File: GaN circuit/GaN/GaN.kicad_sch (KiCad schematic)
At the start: 1 part, among them IC1 LTC7891RUFDM#PBF

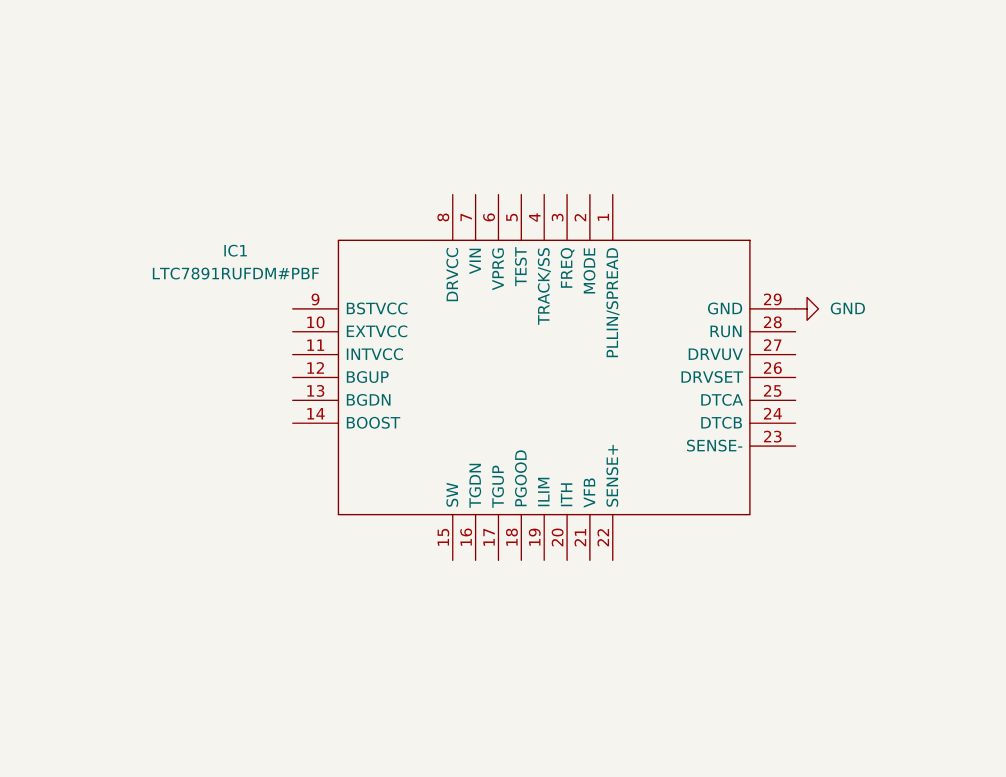
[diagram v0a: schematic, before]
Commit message: Began wiring the PCB for the GaN circuit
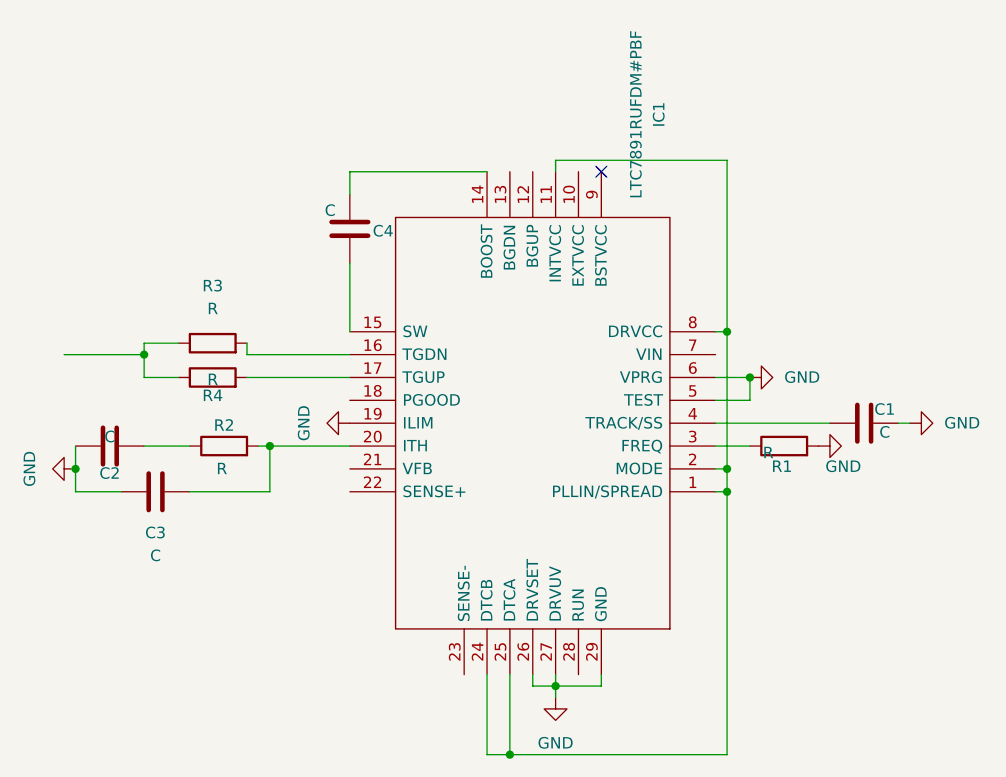
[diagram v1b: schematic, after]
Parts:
- added C1, C2, C3, C4: C, symbol Device:C
- added R1, R2, R3, R4: R, symbol Device:R
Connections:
- net GND: now also IC1.19 (ILIM), IC1.26 (DRVSET), IC1.27 (DRVUV), IC1.5 (TEST), IC1.6 (VPRG), C1.2, C2.1, C3.1, R1.2
- net at IC1.1 (PLLIN/SPREAD): now also IC1.11 (INTVCC), IC1.2 (MODE), IC1.24 (DTCB), IC1.25 (DTCA), IC1.8 (DRVCC)
- net at IC1.14 (BOOST): now also C4.1
- net at IC1.15 (SW): now also C4.2
- net at IC1.16 (TGDN): now also R3.2
- net at IC1.17 (TGUP): now also R4.2
- net at IC1.20 (ITH): now also C3.2, R2.2
- net at IC1.3 (FREQ): now also R1.1
- net at IC1.4 (TRACK/SS): now also C1.1
- new net: C2.2, R2.1
- new net: R3.1, R4.1
- no-connect marks 0 -> 1
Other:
- moved on the sheet: IC1

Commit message: Finished GaN schematic
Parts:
- removed R1: R, symbol Device:R
- added C10, C11, C14, C5, C6, C7, C8, C9: C, symbol Device:C
- added C12, C13, C15: C_US, symbol Device:C_US
- added L1: L, symbol Device:L
- added Q1, Q2: EPC2001C, EPC_FETs:D0188, symbol EPC_FETs:EPC2001C
- added R10, R11, R5, R6, R7, R8, R9: R, symbol Device:R
- added V2: 1, symbol Simulation_SPICE:VDC
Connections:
- net GND: now also IC1.1 (PLLIN/SPREAD), IC1.3 (FREQ), C10.2, C11.2, C12.2, C13.2, C14.2, C15.2, C5.1, C6.1, C8.2, C9.2, Q2.10 (S4), Q2.2 (Sub), Q2.4 (S1), Q2.6 (S2), Q2.8 (S3), R11.2, R9.2, V2.2; no longer IC1.19 (ILIM)
- net ITH: now reaches C3.2, IC1.20 (ITH), R2.2
- net at R3.1, R4.1: now also Q1.1 (G)
- net TGUP: now reaches IC1.17 (TGUP), R4.2
- net INTVCC: now reaches IC1.11 (INTVCC), IC1.2 (MODE), IC1.24 (DTCB), IC1.25 (DTCA), IC1.8 (DRVCC)
- net INTVCC: now also C6.2, R5.2; no longer IC1.1 (PLLIN/SPREAD)
- net OUT: now reaches IC1.10 (EXTVCC)
- net OUT: now also IC1.21 (VFB), IC1.23 (SENSE-), C10.1, C11.1, C12.1, C13.1, C7.2, C8.1, C9.1, R8.1, R9.1
- net BGUP: now reaches IC1.12 (BGUP)
- net BGUP: now also R6.1
- net BGDN: now reaches IC1.13 (BGDN)
- net BOOST: now reaches C4.1, IC1.14 (BOOST)
- net SW: now reaches C4.2, IC1.15 (SW)
- net SW: now also L1.1, Q1.10 (S4), Q1.2 (Sub), Q1.4 (S1), Q1.6 (S2), Q1.8 (S3), Q2.11 (D5), Q2.3 (D1), Q2.5 (D2), Q2.7 (D3), Q2.9 (D4)
- net TGDN: now reaches IC1.16 (TGDN), R3.2
- net PGOOD: now reaches IC1.18 (PGOOD)
- net PGOOD: now also R5.1
- net SENSE+: now reaches IC1.22 (SENSE+)
- net SENSE+: now also C7.1, L1.2, R8.2
- net RUN: now reaches IC1.28 (RUN)
- net RUN: now also C14.1, R10.2, R11.1
- net VIN: now reaches IC1.7 (VIN)
- net VIN: now also C15.1, C5.2, Q1.11 (D5), Q1.3 (D1), Q1.5 (D2), Q1.7 (D3), Q1.9 (D4), R10.1, V2.1
- new net: Q2.1 (G), R6.2, R7.2
- new net BUDN: R7.1
- no-connect marks 1 -> 2
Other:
- moved on the sheet: C1, C2, C3, C4, IC1, R2, R3, R4

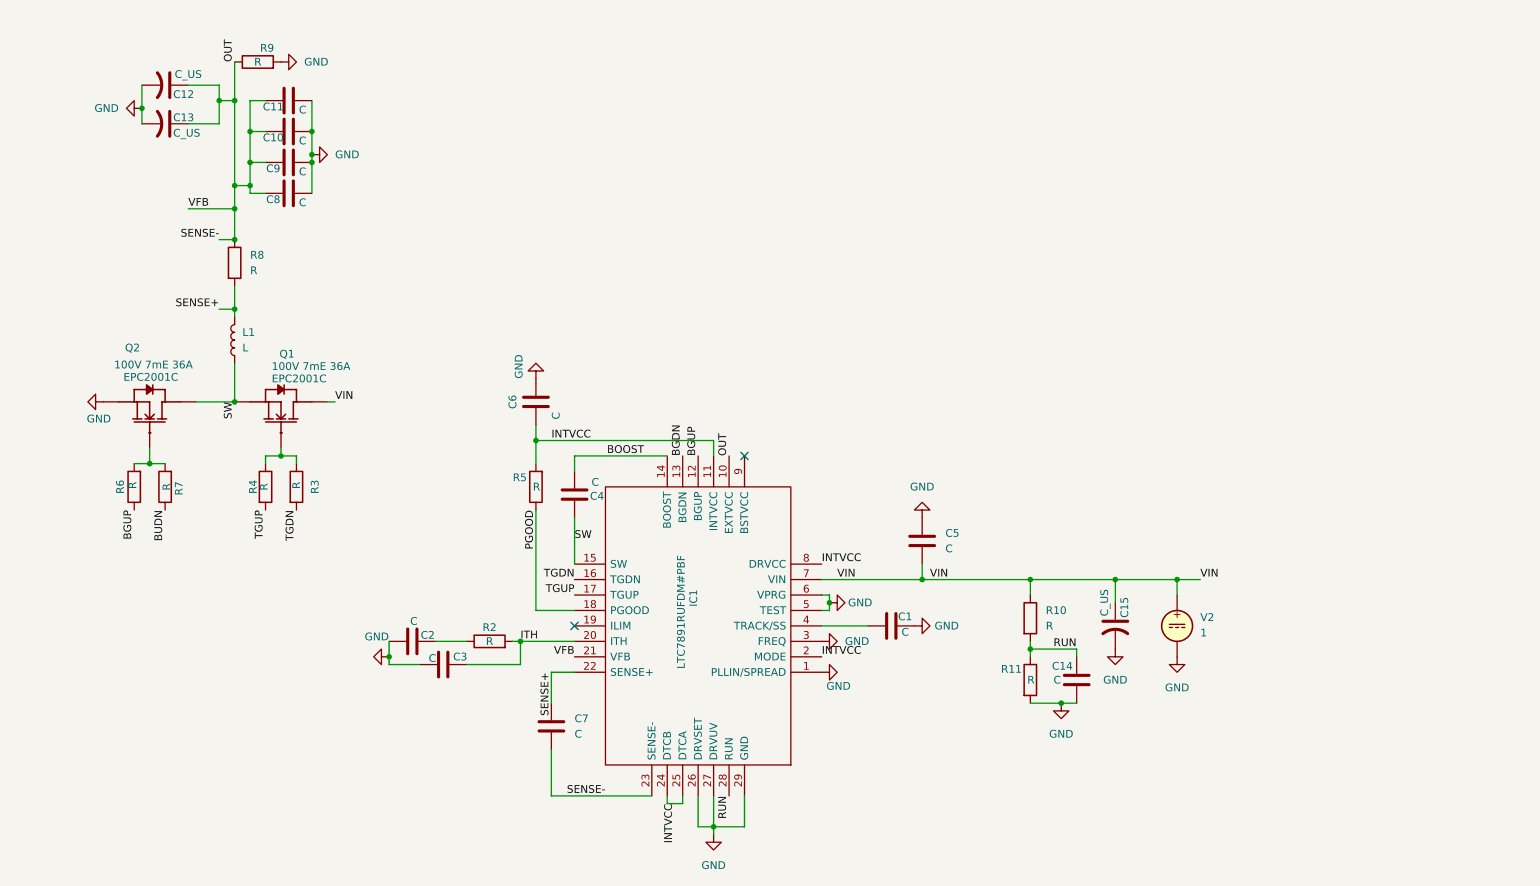
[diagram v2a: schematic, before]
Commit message: Assigned values to parts, replaced inductor with CoilCraft one
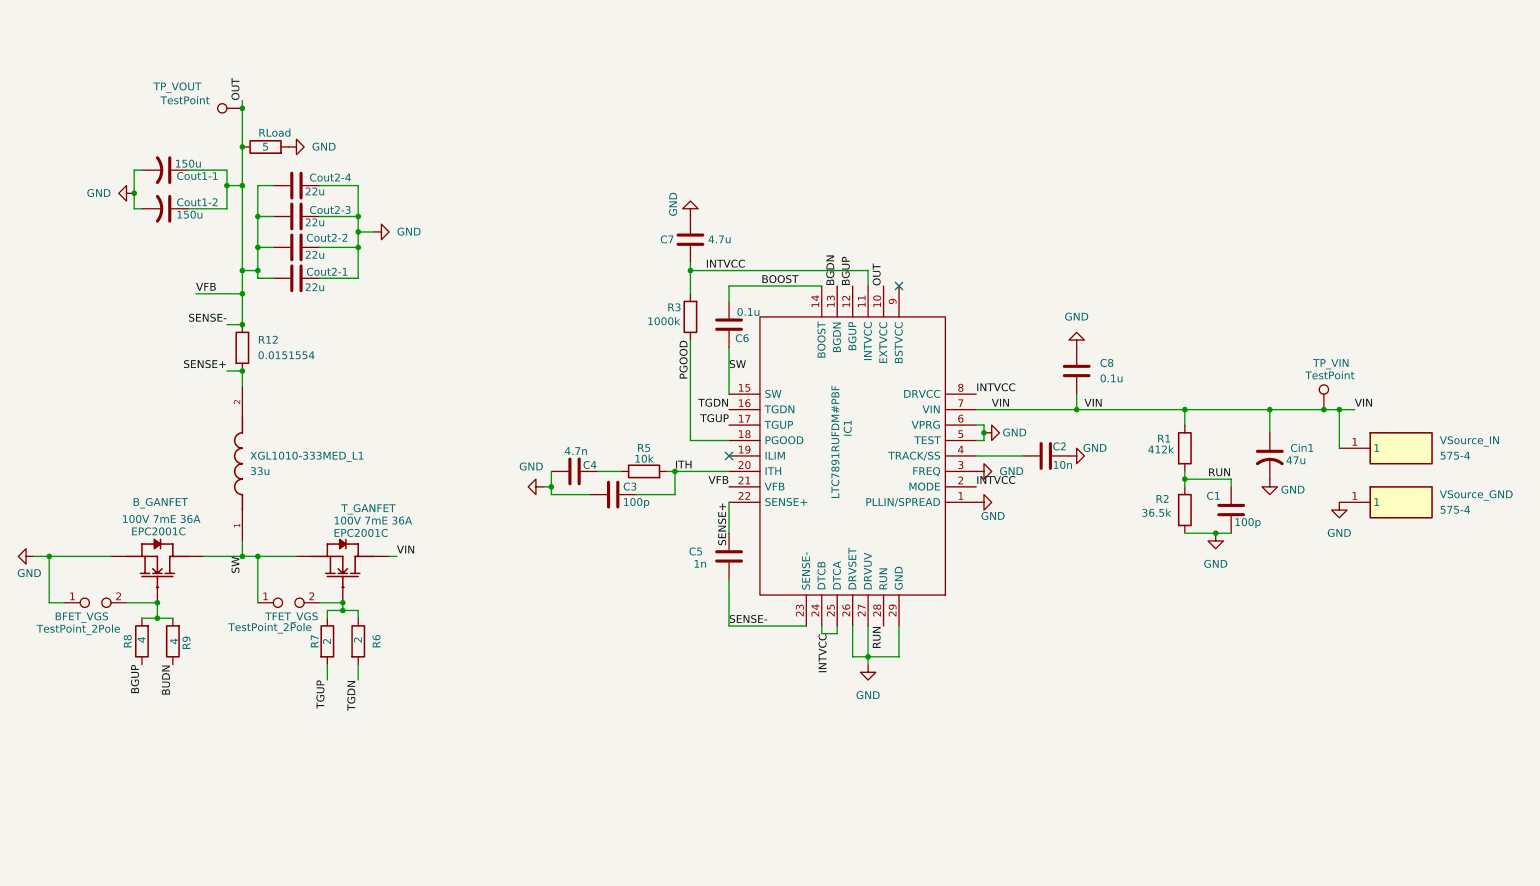
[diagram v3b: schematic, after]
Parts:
- removed L1: L, symbol Device:L
- removed V2: 1, symbol Simulation_SPICE:VDC
- added BFET_VGS, TFET_VGS: TestPoint_2Pole, symbol Connector:TestPoint_2Pole
- added TP_VIN, TP_VOUT: TestPoint, symbol Connector:TestPoint
- added VSource_GND, VSource_IN: 575-4, 5754, symbol 575-4:575-4
- added XGL1010-333MED_L1: 33u, XGL1010-333MED:IND_XGL1010-333MED, symbol XGL1010-333MED:XGL1010-333MED
- C1: renamed from C14; value C -> 100p
- C2: renamed from C1; value C -> 10n
- C3: value C -> 100p
- C4: renamed from C2; value C -> 4.7n
- C5: renamed from C7; value C -> 1n
- C6: renamed from C4; value C -> 0.1u
- C7: renamed from C6; value C -> 4.7u
- C8: renamed from C5; value C -> 0.1u
- Cin1: renamed from C15; value C_US -> 47u
- Cout1-1: renamed from C12; value C_US -> 150u
- Cout1-2: renamed from C13; value C_US -> 150u
- Cout2-1: renamed from C8; value C -> 22u
- Cout2-2: renamed from C9; value C -> 22u
- Cout2-3: renamed from C10; value C -> 22u
- Cout2-4: renamed from C11; value C -> 22u
- R1: renamed from R10; value R -> 412k
- R12: renamed from R8; value R -> 0.0151554
- R2: renamed from R11; value R -> 36.5k
- R3: renamed from R5; value R -> 1000k
- R5: renamed from R2; value R -> 10k
- R6: renamed from R3; value R -> 2
- R7: renamed from R4; value R -> 2
- R8: renamed from R6; value R -> 4
- R9: renamed from R7; value R -> 4
- RLoad: renamed from R9; value R -> 5
- renumbered Q2 to B_GANFET, Q1 to T_GANFET
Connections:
- net GND: now also BFET_VGS.1, VSource_GND.1
- net OUT: now also TP_VOUT.1
- net SENSE+: now also XGL1010-333MED_L1.2
- net SW: now also TFET_VGS.1, XGL1010-333MED_L1.1
- net VIN: now also TP_VIN.1, VSource_IN.1
- net at B_GANFET.1 (G), R8.2, R9.2: now also BFET_VGS.2
- net at R6.1, R7.1, T_GANFET.1 (G): now also TFET_VGS.2
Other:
- moved on the sheet: B_GANFET, C1, C2, C3, C4, C5, C6, C7, C8, Cin1, Cout1-1, Cout1-2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
